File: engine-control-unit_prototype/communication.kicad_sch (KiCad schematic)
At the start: 40 parts, among them J1 JTAG, J2 USB_C_Receptacle_USB2.0_man, J25 I2C_TPS3V3, J27 I2C_TPS10V, J28 I2C_CM, J29 I2C, J8 FDCAN, J9 ADXL345, Q1 PMOS, U1 USBLC6-2SC6, U5 TCAN337G

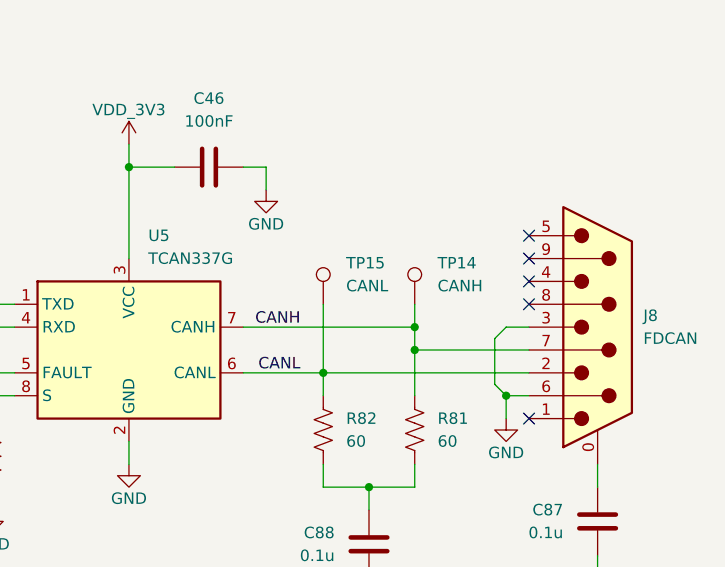
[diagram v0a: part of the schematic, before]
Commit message: Added subsheets
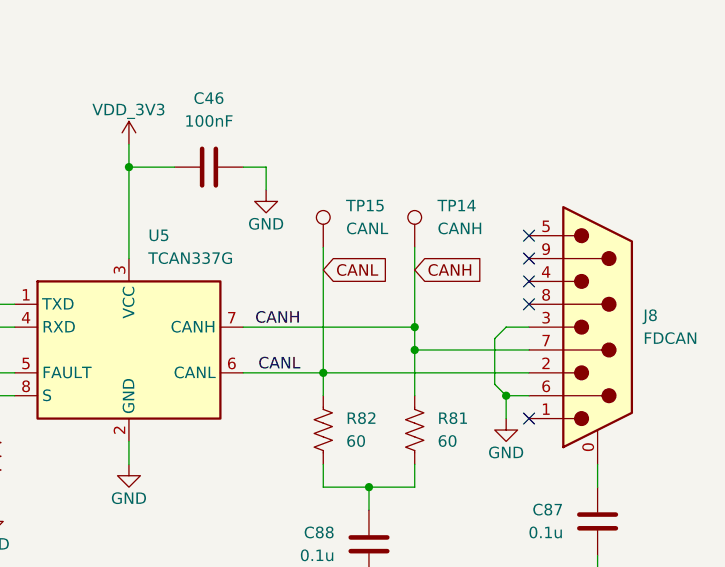
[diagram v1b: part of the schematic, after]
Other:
- moved on the sheet: TP14, TP15
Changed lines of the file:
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@@
 	(wire
 		(pts
-			(xy 237.49 118.11) (xy 237.49 120.65)
+			(xy 237.49 111.76) (xy 237.49 120.65)
 		)
 		(stroke
@@
 	(wire
 		(pts
-			(xy 227.33 118.11) (xy 227.33 125.73)
-		)
-		(stroke
-			(width 0)
-			(type default)
-		)
-	)
-	(wire
-		(pts
 			(xy 26.67 53.34) (xy 58.42 53.34)
 		)
@@
 	(wire
 		(pts
+			(xy 227.33 111.76) (xy 227.33 125.73)
+		)
+		(stroke
+			(width 0)
+			(type default)
+		)
+	)
+	(wire
+		(pts
 			(xy 116.84 170.18) (xy 116.84 172.72)
 		)
@@
 		)
 	)
+	(global_label "CANH"
+		(shape input)
+		(at 237.49 114.3 0)
+		(fields_autoplaced yes)
+		(effects
+			(font
+				(size 1.27 1.27)
+			)
+			(justify left)
+		)
+		(property "Intersheetrefs" "${INTERSHEET_REFS}"
+			(at 245.4948 114.3 0)
+			(effects
+				(font
+					(size 1.27 1.27)
+				)
+				(justify left)
+				(hide yes)
+			)
+		)
+	)
+	(global_label "CANL"
+		(shape input)
+		(at 227.33 114.3 0)
+		(fields_autoplaced yes)
+		(effects
+			(font
+				(size 1.27 1.27)
+			)
+			(justify left)
+		)
+		(property "Intersheetrefs" "${INTERSHEET_REFS}"
+			(at 235.0324 114.3 0)
+			(effects
+				(font
+					(size 1.27 1.27)
+				)
+				(justify left)
+				(hide yes)
+			)
+		)
+	)
 	(hierarchical_label "TPS3V3_SCL"
 		(shape input)
@@
 	(symbol
 		(lib_id "Connector:TestPoint")
-		(at 237.49 118.11 0)
+		(at 237.49 111.76 0)
 		(unit 1)
 		(exclude_from_sim no)
@@
 		(fields_autoplaced yes)
 		(property "Reference" "TP14"
-			(at 240.03 113.5379 0)
+			(at 240.03 107.1879 0)
 			(effects
 				(font
@@
 		)
 		(property "Value" "CANH"
-			(at 240.03 116.0779 0)
+			(at 240.03 109.7279 0)
 			(effects
 				(font
@@
 		)
 		(property "Footprint" ""
-			(at 242.57 118.11 0)
+			(at 242.57 111.76 0)
 			(effects
 				(font
@@
 		)
 		(property "Datasheet" "~"
-			(at 242.57 118.11 0)
+			(at 242.57 111.76 0)
 			(effects
 				(font
@@
 		)
 		(property "Description" "test point"
-			(at 237.49 118.11 0)
+			(at 237.49 111.76 0)
 			(effects
 				(font
@@
 	(symbol
 		(lib_id "Connector:TestPoint")
-		(at 227.33 118.11 0)
+		(at 227.33 111.76 0)
 		(unit 1)
 		(exclude_from_sim no)
@@
 		(fields_autoplaced yes)
 		(property "Reference" "TP15"
-			(at 229.87 113.5379 0)
+			(at 229.87 107.1879 0)
 			(effects
 				(font
@@
 		)
 		(property "Value" "CANL"
-			(at 229.87 116.0779 0)
+			(at 229.87 109.7279 0)
 			(effects
 				(font
@@
 		)
 		(property "Footprint" ""
-			(at 232.41 118.11 0)
+			(at 232.41 111.76 0)
 			(effects
 				(font
@@
 		)
 		(property "Datasheet" "~"
-			(at 232.41 118.11 0)
+			(at 232.41 111.76 0)
 			(effects
 				(font
@@
 		)
 		(property "Description" "test point"
-			(at 227.33 118.11 0)
+			(at 227.33 111.76 0)
 			(effects
 				(font

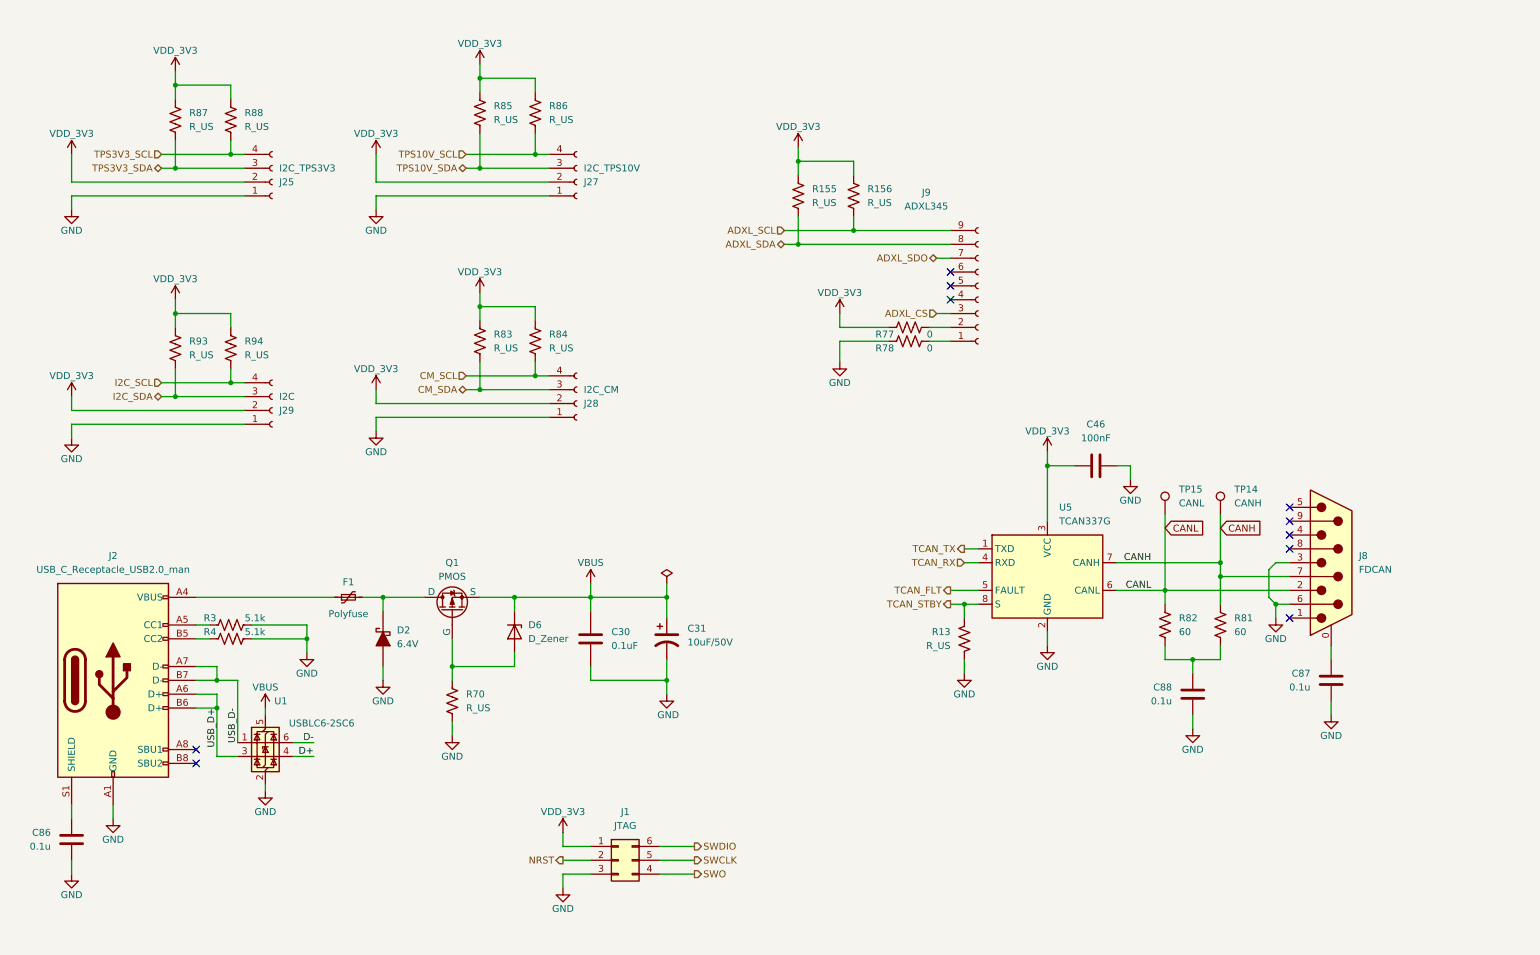
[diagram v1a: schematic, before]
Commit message: Added Control page Revisited power tree (VDDA_3V3 and VDD_3V3) Bunch of other fixes
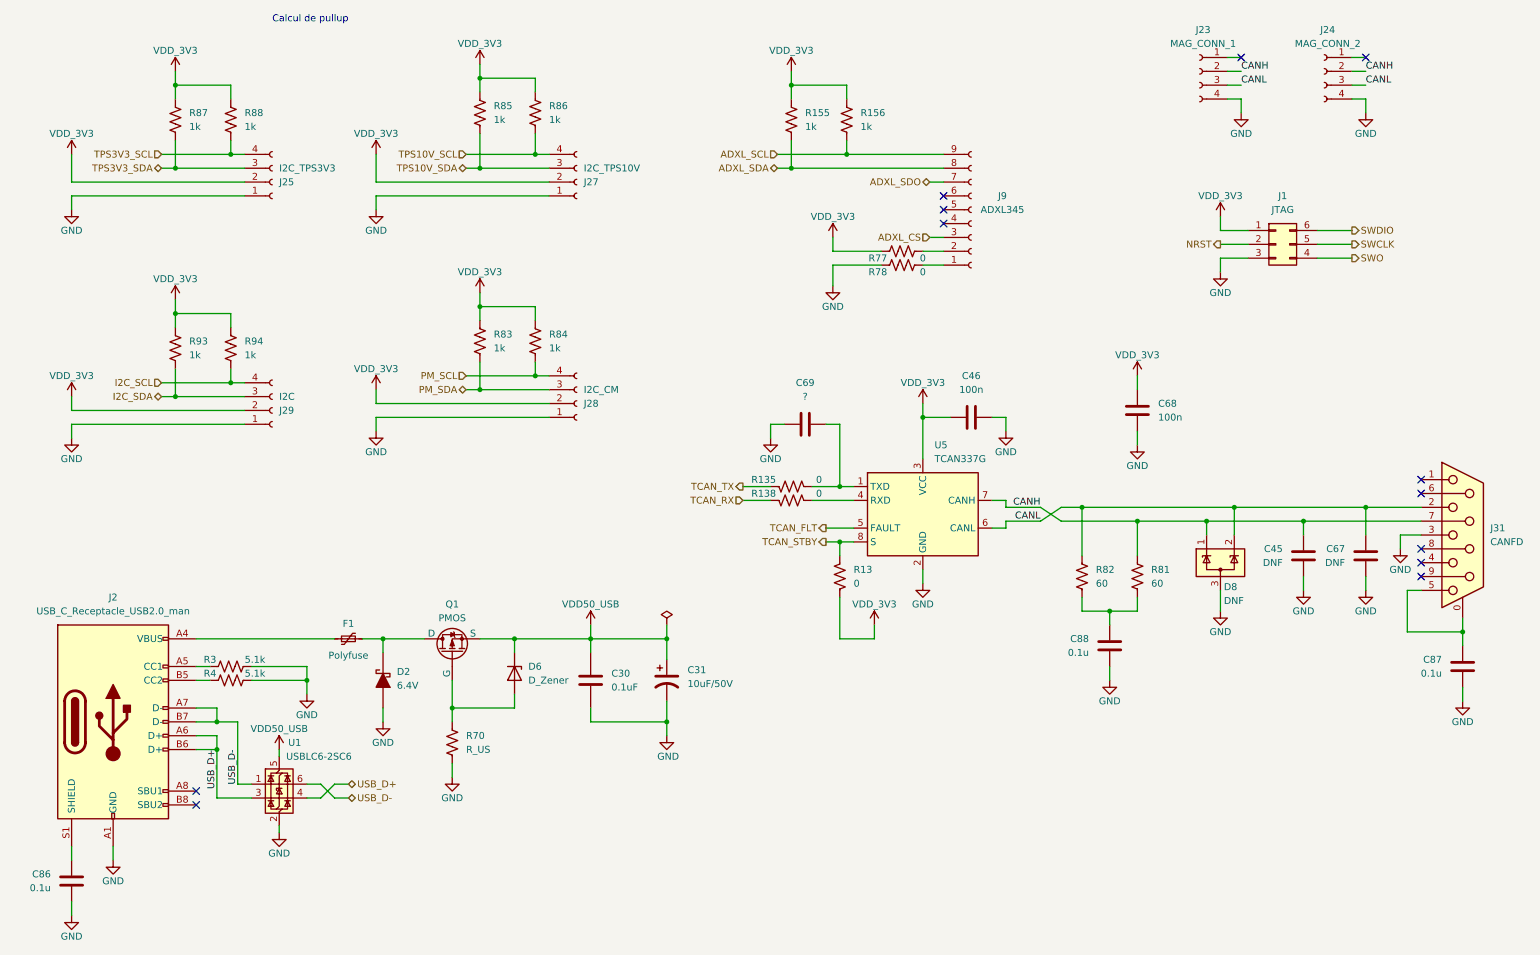
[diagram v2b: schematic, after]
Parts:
- removed J8: FDCAN, symbol Connector:DE9_Pins_MountingHoles
- removed TP14: CANH, symbol Connector:TestPoint
- removed TP15: CANL, symbol Connector:TestPoint
- added C45, C67: DNF, Capacitor_SMD:C_0603_1608Metric, symbol Device:C
- added C68: 100n, Capacitor_SMD:C_0603_1608Metric, symbol Device:C
- added C69: ?, Capacitor_SMD:C_0603_1608Metric, symbol Device:C
- added D8: DNF, Package_TO_SOT_SMD:SOT-23-3, symbol Power_Protection:ESDA5V3L
- added J23: MAG_CONN_1, symbol Connector:Conn_01x04_Socket
- added J24: MAG_CONN_2, symbol Connector:Conn_01x04_Socket
- added J31: CANFD, symbol Connector:DE9_Socket_MountingHoles
- added R135, R138: 0, Resistor_SMD:R_0603_1608Metric, symbol Device:R_US
- C30: footprint Capacitor_SMD:C_0603_1608Metric_Pad1.08x0.95mm_HandSolder -> Capacitor_SMD:C_0603_1608Metric
- C46: value 100nF -> 100n; footprint (none) -> Capacitor_SMD:C_0603_1608Metric
- C86, C87, C88: footprint (none) -> Capacitor_SMD:C_0603_1608Metric
- R13: value R_US -> 0; footprint (none) -> Resistor_SMD:R_0603_1608Metric
- R155, R156, R83, R84, R85, R86, R87, R88, R93, R94: value R_US -> 1k; footprint (none) -> Resistor_SMD:R_0402_1005Metric
- R3, R4, R70, R81, R82: footprint (none) -> Resistor_SMD:R_0603_1608Metric
- R77, R78: footprint (none) -> Resistor_SMD:R_0201_0603Metric
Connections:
- net D+ is gone; now on net USB_D+: U1.4 (I/O2)
- net D- is gone; now on net USB_D-: U1.6 (I/O1)
- net CANH: now also C45.2, D8.1 (K), J23.2 (Pin_2), J24.2 (Pin_2), J31.7
- net CANL: now also C67.2, D8.2 (K), J23.3 (Pin_3), J24.3 (Pin_3), J31.2
- net GND: now also C45.1, C67.1, C68.1, C69.1, D8.3 (A), J23.4 (Pin_4), J24.4 (Pin_4), J31.3; no longer R13.2
- net TCAN_RX: now also R138.1; no longer U5.4 (RXD)
- net TCAN_TX: now also R135.1; no longer U5.1 (TXD)
- net VDD_3V3: now also R13.2, C68.2
- net at C87.2: now also J31.0 (PAD), J31.5
- net CM_SCL renamed PM_SCL
- net CM_SDA renamed PM_SDA
- net VBUS renamed VDD50_USB
- new net: C69.2, R135.2, U5.1 (TXD)
- new net: R138.2, U5.4 (RXD)
- no-connect marks 10 -> 12
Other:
- note added: "Calcul de pullup"
- moved on the sheet: C30, C31, C46, C86, C87, C88, D2, D6, F1, J1, J2, J9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

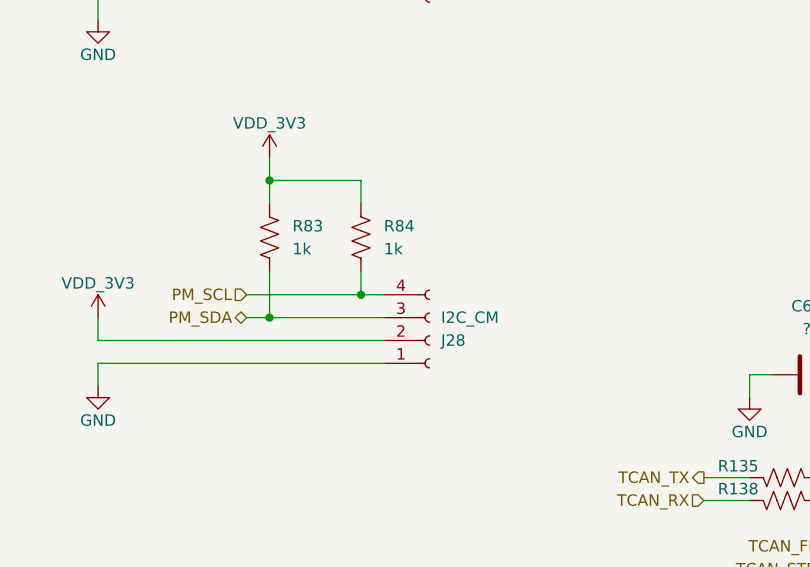
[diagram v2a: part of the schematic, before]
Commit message: Fixed inverted LED diodes (oops) Replaced 3x INA219 with INA3221
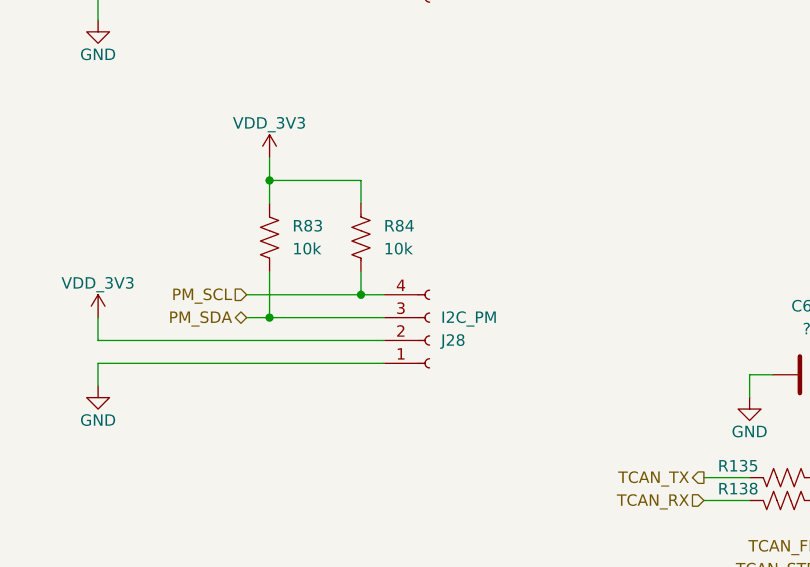
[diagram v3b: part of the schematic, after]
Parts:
- J28: value I2C_CM -> I2C_PM
- R83, R84: value 1k -> 10k
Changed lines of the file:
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@@
 			)
 		)
-		(property "Value" "I2C_CM"
+		(property "Value" "I2C_PM"
 			(at 120.65 88.9001 0)
 			(effects
@@
 			)
 		)
-		(property "Value" "1k"
+		(property "Value" "10k"
 			(at 114.3 81.2799 0)
 			(effects
@@
 			)
 		)
-		(property "Value" "1k"
+		(property "Value" "10k"
 			(at 104.14 81.2799 0)
 			(effects

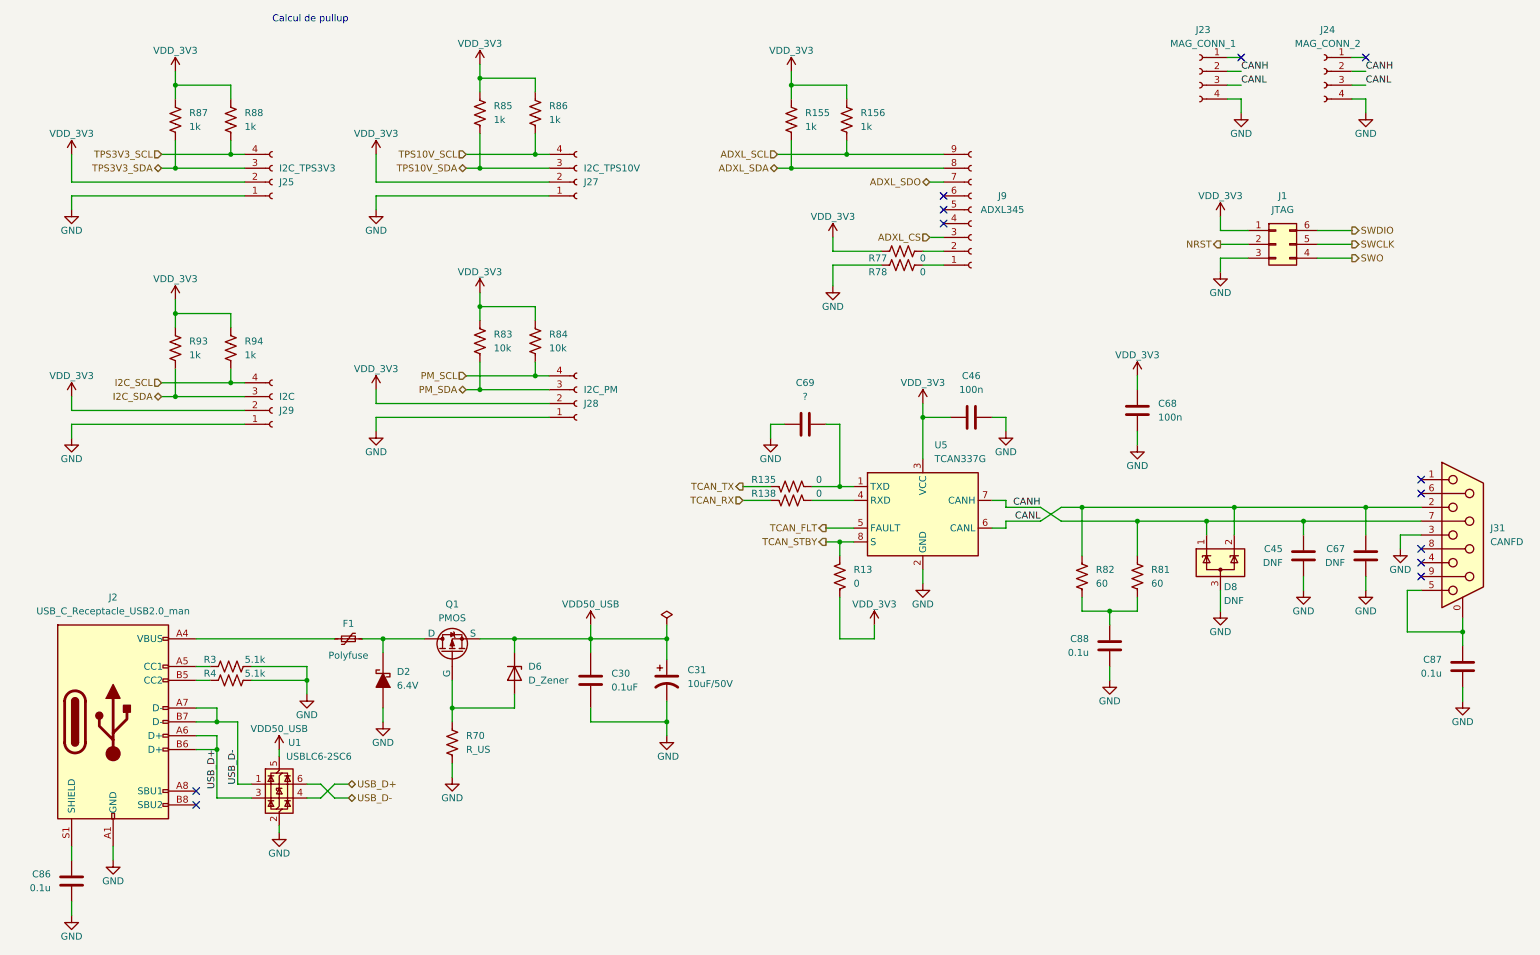
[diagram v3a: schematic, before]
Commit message: Added magnetic encoders Added optional external valve control connector
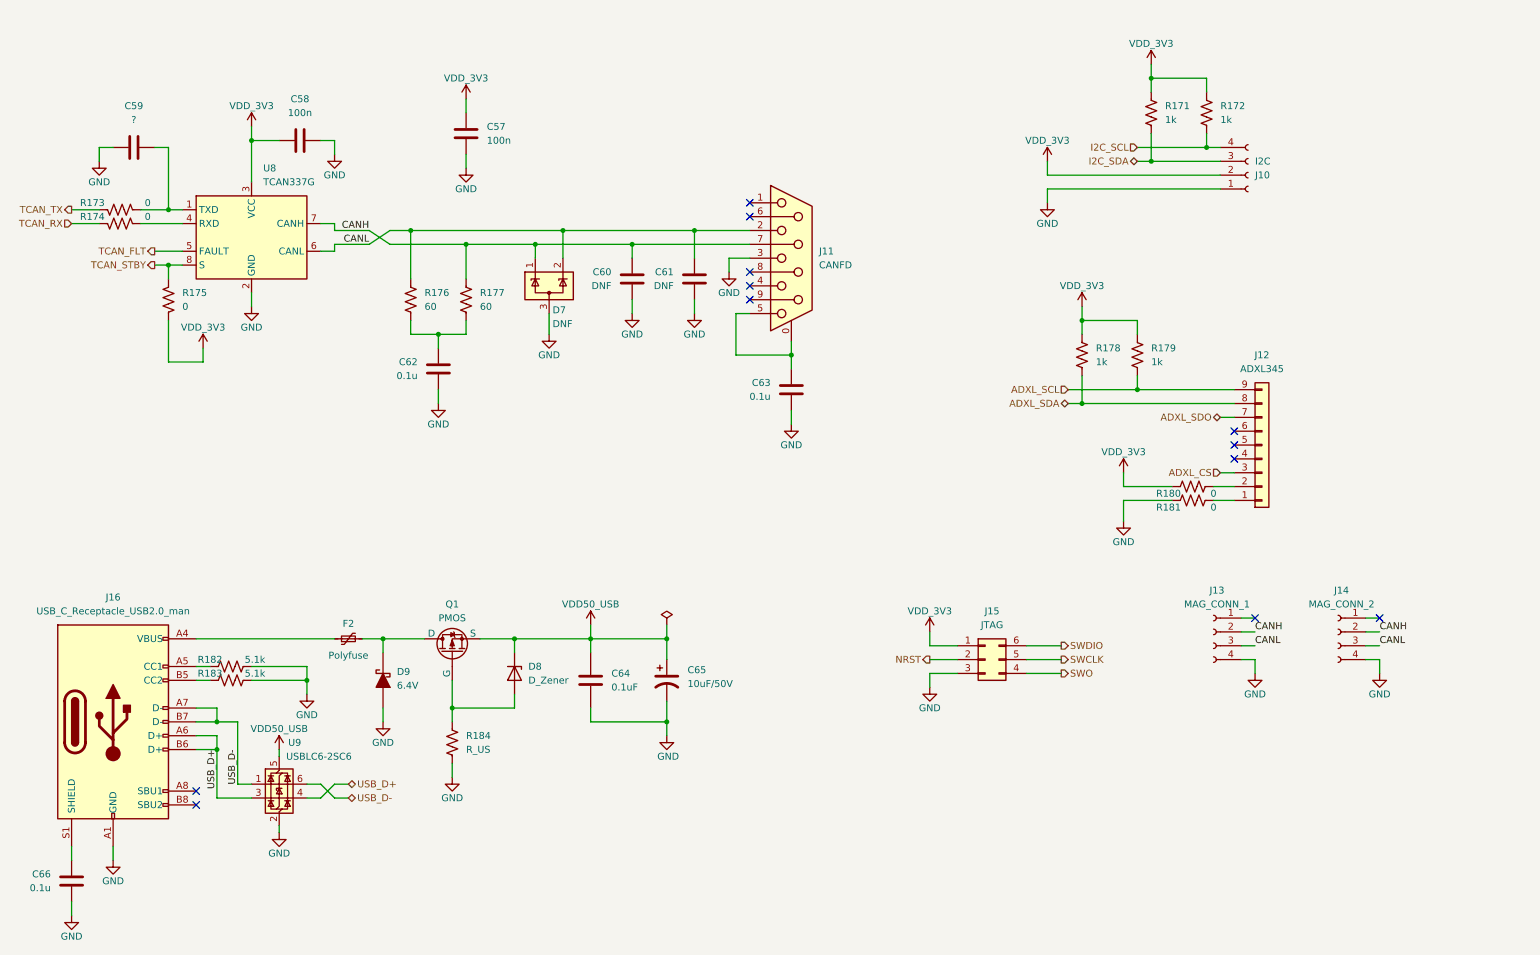
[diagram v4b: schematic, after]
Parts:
- removed J25: I2C_TPS3V3, symbol Connector:Conn_01x04_Socket
- removed J27: I2C_TPS10V, symbol Connector:Conn_01x04_Socket
- removed J28: I2C_PM, symbol Connector:Conn_01x04_Socket
- removed J9: ADXL345, symbol Connector:Conn_01x09_Socket
- removed R83, R84: 10k, Resistor_SMD:R_0402_1005Metric, symbol Device:R_US
- removed R85, R86, R87, R88: 1k, Resistor_SMD:R_0402_1005Metric, symbol Device:R_US
- added J12: ADXL345, symbol Connector_Generic:Conn_01x09
- renumbered C68 to C57, C46 to C58, C69 to C59, C45 to C60, C67 to C61, C88 to C62, C87 to C63, C30 to C64, C31 to C65, C86 to C66, D8 to D7, D6 to D8, D2 to D9, F1 to F2, J29 to J10, J31 to J11, J23 to J13, J24 to J14, J1 to J15, J2 to J16, R93 to R171, R94 to R172, R135 to R173, R138 to R174, R13 to R175, R82 to R176, R81 to R177, R155 to R178, R156 to R179, R77 to R180, R78 to R181, R3 to R182, R4 to R183, R70 to R184, U5 to U8, U1 to U9
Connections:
- net ADXL_CS: now also J12.3 (Pin_3)
- net ADXL_SCL: now also J12.9 (Pin_9)
- net ADXL_SDA: now also J12.8 (Pin_8)
- net ADXL_SDO: now also J12.7 (Pin_7)
- net at R181.2: now also J12.1 (Pin_1)
- net at R180.2: now also J12.2 (Pin_2)
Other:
- note removed: "Calcul de pullup"
- moved on the sheet: C57, C58, C59, C60, C61, C62, C63, D7, J10, J11, J13, J14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
